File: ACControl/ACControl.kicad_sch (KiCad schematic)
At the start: 18 parts, among them J1 Conn_02x08_Odd_Even, J2 DG300-5.0-02P13, J3 DG300-5.0-02P13, K1 AZ921-1A-12DE, K2 AZ921-1A-12DE, Q1 BC848, Q2 BC848, U1 SFH6156-1T, U2 SFH6156-1T

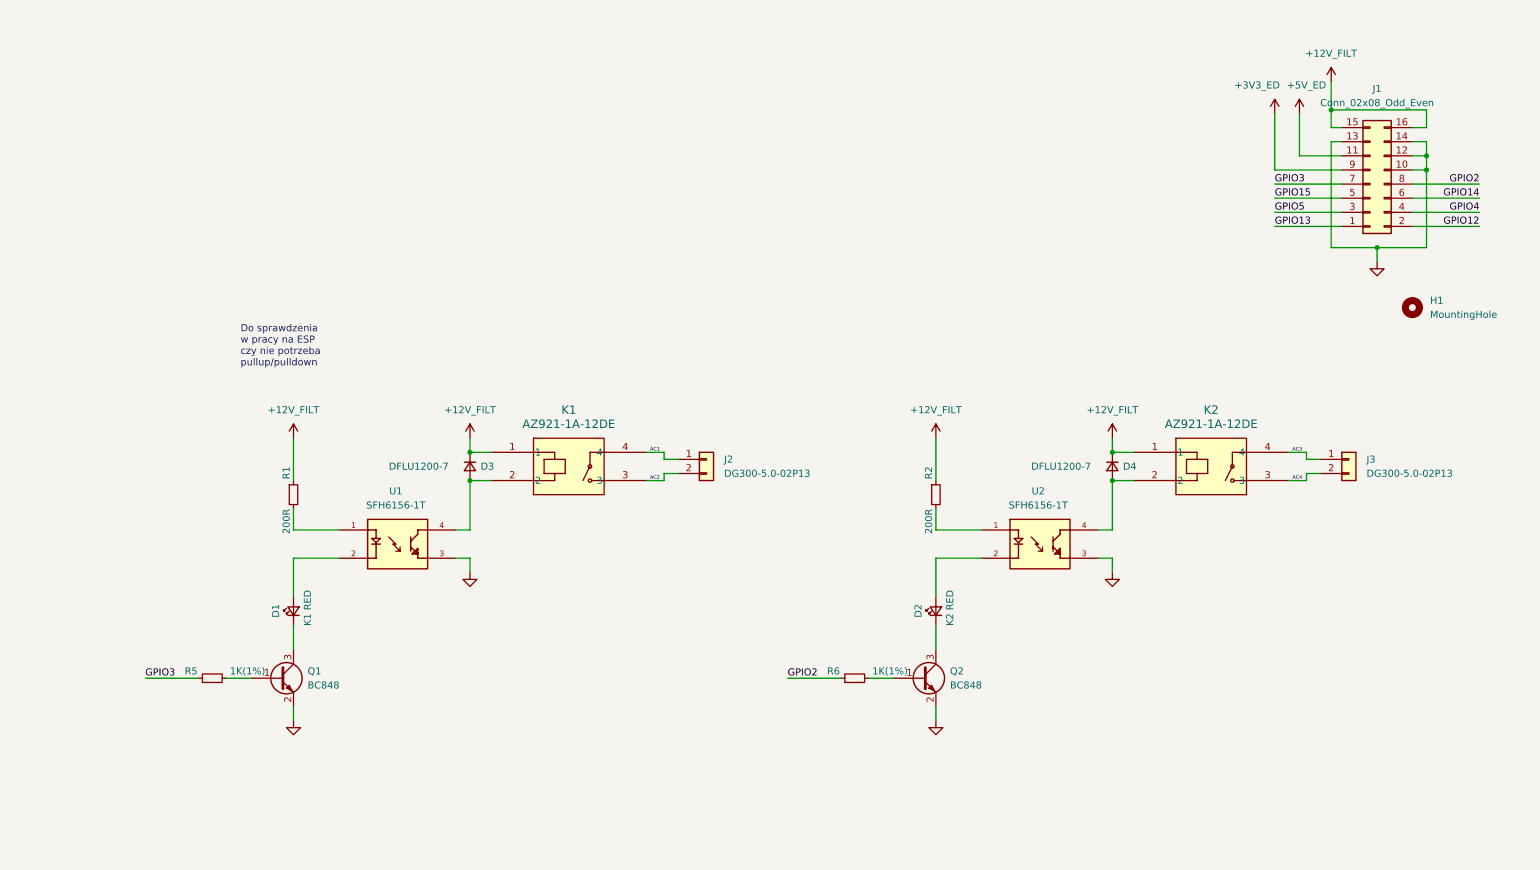
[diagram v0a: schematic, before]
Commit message: Structure changes to schematic files
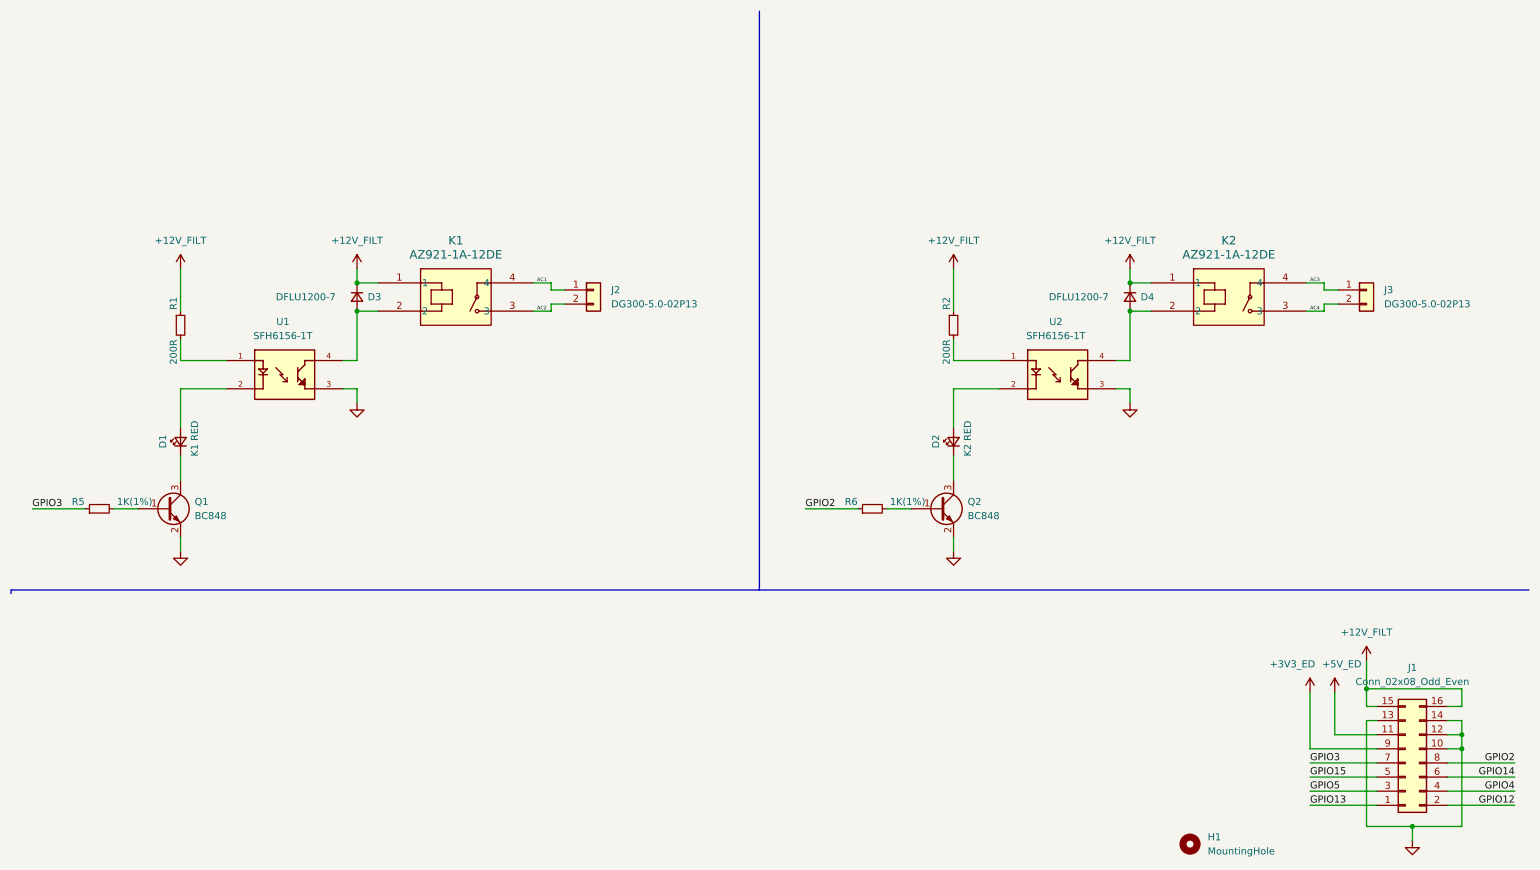
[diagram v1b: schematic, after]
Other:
- note removed: "Do sprawdzenia w pracy na ESP czy nie potrzeba pullup/pulldown"
- moved on the sheet: D1, D2, D3, D4, H1, J1, J2, J3, K1, K2, Q1, Q2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
